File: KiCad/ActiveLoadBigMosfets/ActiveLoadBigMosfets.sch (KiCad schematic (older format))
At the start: 190 parts, among them J1 TouchPanel, J10 I2C, J2 PowerInput, J3 SWD, J4 RVT28AETNWC00, J5 JTAG, J6 FanOut, J7 PowerInput2, J8 PowerInput3, J9 PowerInput4, Q1 IRLML2502, Q10 IXFK44N50P, Q11 IXFK44N50P, Q12 IXFK44N50P, Q13 IXFK44N50P, Q14 IXFK44N50P, Q15 IRLML2244, Q16 IRLML2244, Q17 IRLML2502, Q2 IRLML2244, Q3 IRLML2244, Q4 IRLML2502, Q5 IRLML2502, Q6 IRLML2502, Q7 IRLML2502, Q8 IRLML2502, Q9 IXFK44N50P, SW1 Rotary_Encoder_Switch, SW2 SW_Push, U1 LMR14020, U2 MCP1825S, U3 STM32L151RBTxA, U4 LM2735YMF, U5 TLV2374, U6 TLV2374, U7 TLV2374, U8 TC74, U9 INA233, Y1 16MHz

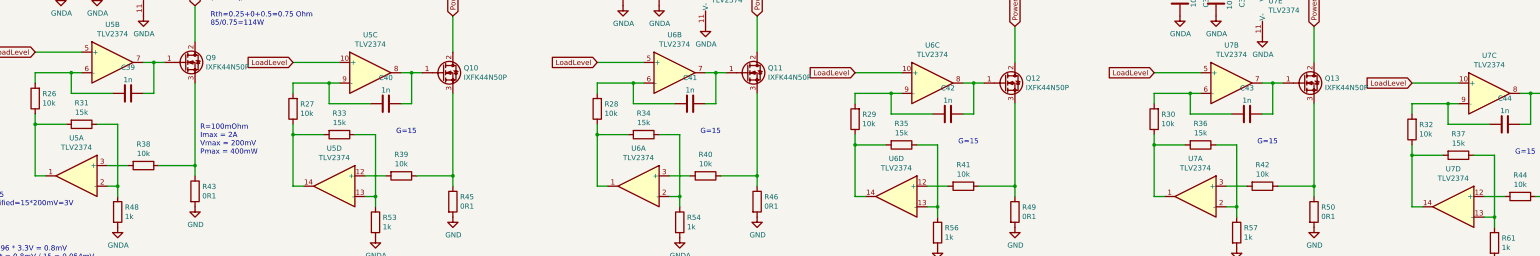
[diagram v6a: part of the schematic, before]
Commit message: Debug screen added
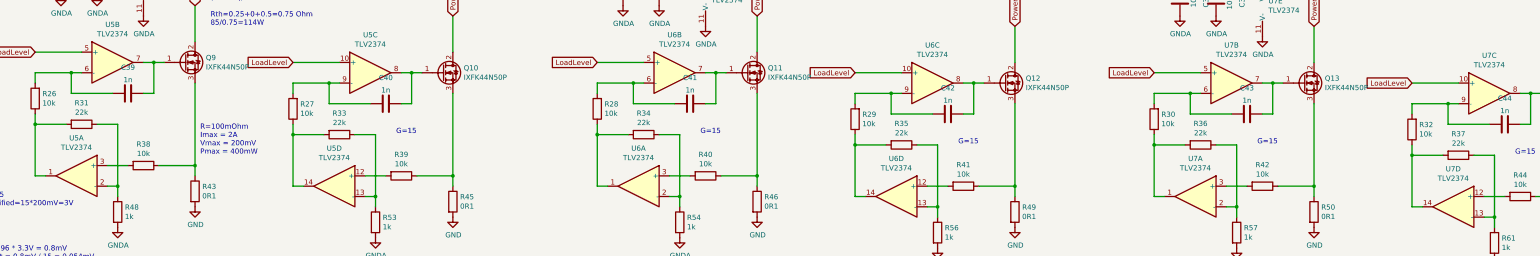
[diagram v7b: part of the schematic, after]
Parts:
- R31, R33, R34, R35, R36, R37: value 15k -> 22k
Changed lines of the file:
@@
 P 7450 9550
 F 0 "R31" V 7243 9550 50  0000 C CNN
-F 1 "15k" V 7334 9550 50  0000 C CNN
+F 1 "22k" V 7334 9550 50  0000 C CNN
 F 2 "Resistor_SMD:R_0805_2012Metric" V 7380 9550 50  0001 C CNN
 F 3 "~" H 7450 9550 50  0001 C CNN
@@
 P 9950 9650
 F 0 "R33" V 9743 9650 50  0000 C CNN
-F 1 "15k" V 9834 9650 50  0000 C CNN
+F 1 "22k" V 9834 9650 50  0000 C CNN
 F 2 "Resistor_SMD:R_0805_2012Metric" V 9880 9650 50  0001 C CNN
 F 3 "~" H 9950 9650 50  0001 C CNN
@@
 P 12900 9650
 F 0 "R34" V 12693 9650 50  0000 C CNN
-F 1 "15k" V 12784 9650 50  0000 C CNN
+F 1 "22k" V 12784 9650 50  0000 C CNN
 F 2 "Resistor_SMD:R_0805_2012Metric" V 12830 9650 50  0001 C CNN
 F 3 "~" H 12900 9650 50  0001 C CNN
@@
 P 15400 9750
 F 0 "R35" V 15193 9750 50  0000 C CNN
-F 1 "15k" V 15284 9750 50  0000 C CNN
+F 1 "22k" V 15284 9750 50  0000 C CNN
 F 2 "Resistor_SMD:R_0805_2012Metric" V 15330 9750 50  0001 C CNN
 F 3 "~" H 15400 9750 50  0001 C CNN
@@
 P 18300 9750
 F 0 "R36" V 18093 9750 50  0000 C CNN
-F 1 "15k" V 18184 9750 50  0000 C CNN
+F 1 "22k" V 18184 9750 50  0000 C CNN
 F 2 "Resistor_SMD:R_0805_2012Metric" V 18230 9750 50  0001 C CNN
 F 3 "~" H 18300 9750 50  0001 C CNN
@@
 P 20800 9850
 F 0 "R37" V 20593 9850 50  0000 C CNN
-F 1 "15k" V 20684 9850 50  0000 C CNN
+F 1 "22k" V 20684 9850 50  0000 C CNN
 F 2 "Resistor_SMD:R_0805_2012Metric" V 20730 9850 50  0001 C CNN
 F 3 "~" H 20800 9850 50  0001 C CNN
@@
 Text Notes 6000 4000 0    50   ~ 0
 Cl=(Cl1*Cl2)/(Cl1+Cl2) + Cs\nAssuming Cs=6p\nFor Cl=18p\nCl1/2=24p
+Text Notes 5800 4150 0    50   ~ 0
+C25 should be gone (smaller?)
 Wire Bus Line
 	19100 4450 19100 4800
@@
 Wire Bus Line
 	7850 4600 7850 6650
-Text Notes 5800 4150 0    50   ~ 0
-C25 should be gone (smaller?)
 $EndSCHEMATC
